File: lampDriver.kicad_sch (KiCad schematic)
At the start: 70 parts, among them IC8 1ED44175N01BXTSA1, Q2 BC847, Q4 BC807, T4 IMBG120R181M2HXTMA1, U1 OPA2356AIDGKR, U3 LM2901

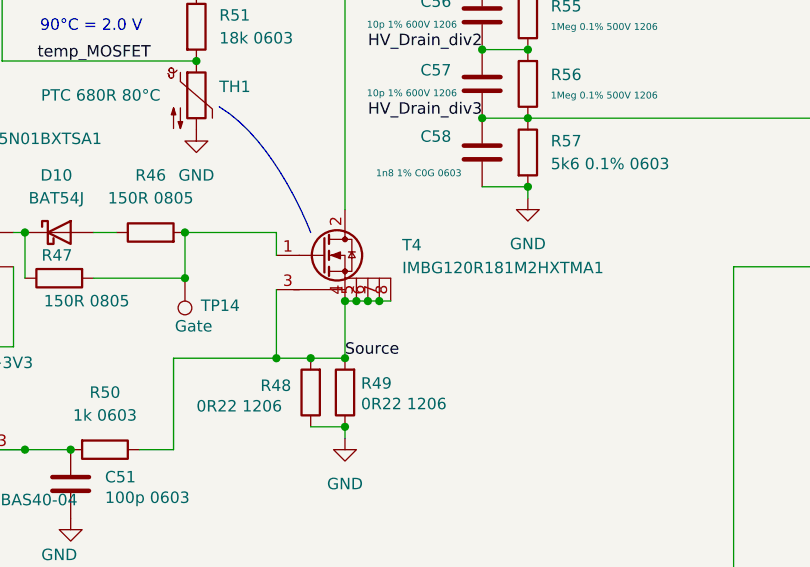
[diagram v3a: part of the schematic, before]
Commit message: changed to THT MOSFET
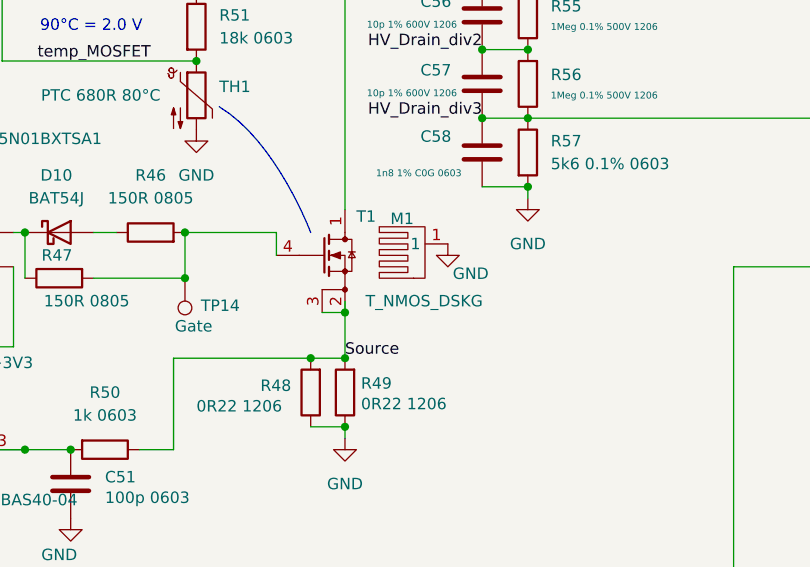
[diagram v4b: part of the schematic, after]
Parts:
- removed T4: IMBG120R181M2HXTMA1, Hansmann:TO-263-7_TabPin2_HV, symbol Hansmann:NMOS_GDS-KS_SMD
- added M1: ~, Hansmann_Kühlkörper:FK 274 MI 247 V, symbol Hansmann_Kühlkörper:Kühlkörper_mit_Pins
- added T1: T_NMOS_DSKG, Package_TO_SOT_THT:TO-247-4_Vertical, symbol Hansmann_Transistoren:Q_NMOS_DSKG
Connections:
- net GND: now also M1.1
- net HV_Drain: now also T1.1 (D)
- net Source: now also T1.2 (S), T1.3 (K)
- net at R46.2, R47.2, TP14.1: now also T1.4 (G)
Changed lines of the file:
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@@
 	)
 	(junction
-		(at 127 91.44)
-		(diameter 0)
-		(color 0 0 0 0)
-	)
-	(junction
-		(at 119.38 97.79)
-		(diameter 0)
-		(color 0 0 0 0)
-	)
-	(junction
 		(at 109.22 83.82)
 		(diameter 0)
@@
 	)
 	(junction
-		(at 130.81 91.44)
-		(diameter 0)
-		(color 0 0 0 0)
-	)
-	(junction
 		(at 123.19 137.16)
 		(diameter 0)
@@
 	)
 	(junction
-		(at 128.27 91.44)
-		(diameter 0)
-		(color 0 0 0 0)
-	)
-	(junction
-		(at 129.54 91.44)
-		(diameter 0)
-		(color 0 0 0 0)
-	)
-	(junction
 		(at 91.44 107.95)
 		(diameter 0)
@@
 	)
 	(junction
+		(at 127 92.71)
+		(diameter 0)
+		(color 0 0 0 0)
+	)
+	(junction
 		(at 242.57 86.36)
 		(diameter 0)
@@
 	(wire
 		(pts
-			(xy 130.81 91.44) (xy 132.08 91.44)
-		)
-		(stroke
-			(width 0)
-			(type default)
-		)
-	)
-	(wire
-		(pts
 			(xy 88.9 54.61) (xy 39.37 54.61)
 		)
@@
 	(wire
 		(pts
-			(xy 119.38 90.17) (xy 119.38 97.79)
-		)
-		(stroke
-			(width 0)
-			(type default)
-		)
-	)
-	(wire
-		(pts
 			(xy 99.06 158.75) (xy 100.33 158.75)
 		)
@@
 	(wire
 		(pts
-			(xy 107.95 97.79) (xy 119.38 97.79)
+			(xy 107.95 97.79) (xy 123.19 97.79)
 		)
 		(stroke
@@
 	(wire
 		(pts
-			(xy 127 91.44) (xy 128.27 91.44)
-		)
-		(stroke
-			(width 0)
-			(type default)
-		)
-	)
-	(wire
-		(pts
 			(xy 118.11 137.16) (xy 123.19 137.16)
 		)
@@
 	(wire
 		(pts
-			(xy 129.54 91.44) (xy 130.81 91.44)
-		)
-		(stroke
-			(width 0)
-			(type default)
-		)
-	)
-	(wire
-		(pts
 			(xy 194.31 46.99) (xy 190.5 46.99)
 		)
@@
 	(wire
 		(pts
-			(xy 127 91.44) (xy 127 97.79)
+			(xy 127 91.44) (xy 127 92.71)
 		)
 		(stroke
@@
 	(wire
 		(pts
-			(xy 119.38 97.79) (xy 123.19 97.79)
-		)
-		(stroke
-			(width 0)
-			(type default)
-		)
-	)
-	(wire
-		(pts
 			(xy 90.17 87.63) (xy 90.17 96.52)
 		)
@@
 	(wire
 		(pts
+			(xy 127 92.71) (xy 127 97.79)
+		)
+		(stroke
+			(width 0.254)
+			(type default)
+		)
+	)
+	(wire
+		(pts
 			(xy 246.38 66.04) (xy 252.73 66.04)
 		)
@@
 	(wire
 		(pts
+			(xy 124.46 92.71) (xy 127 92.71)
+		)
+		(stroke
+			(width 0.254)
+			(type default)
+		)
+	)
+	(wire
+		(pts
 			(xy 147.32 180.34) (xy 147.32 181.61)
 		)
@@
 	(wire
 		(pts
-			(xy 128.27 91.44) (xy 129.54 91.44)
-		)
-		(stroke
-			(width 0)
-			(type default)
-		)
-	)
-	(wire
-		(pts
 			(xy 214.63 100.33) (xy 215.9 100.33)
 		)
@@
 	)
 	(symbol
-		(lib_id "Hansmann:NMOS_GDS-KS_SMD")
-		(at 124.46 86.36 0)
-		(unit 1)
-		(exclude_from_sim no)
-		(in_bom yes)
-		(on_board yes)
-		(dnp no)
-		(fields_autoplaced yes)
-		(property "Reference" "T4"
-			(at 133.35 85.2169 0)
-			(effects
-				(font
-					(size 1.27 1.27)
-				)
-				(justify left)
-			)
-		)
-		(property "Value" "IMBG120R181M2HXTMA1"
-			(at 133.35 87.7569 0)
-			(effects
-				(font
-					(size 1.27 1.27)
-				)
-				(justify left)
-			)
-		)
-		(property "Footprint" "Hansmann:TO-263-7_TabPin2_HV"
-			(at 129.54 83.82 0)
-			(effects
-				(font
-					(size 1.27 1.27)
-				)
-				(hide yes)
-			)
-		)
-		(property "Datasheet" ""
-			(at 124.46 86.36 0)
-			(effects
-				(font
-					(size 1.27 1.27)
-				)
-				(hide yes)
-			)
-		)
-		(property "Description" "N-MOSFET transistor, gate/drain/source"
-			(at 124.46 86.36 0)
-			(effects
-				(font
-					(size 1.27 1.27)
-				)
-				(hide yes)
-			)
-		)
-		(pin "3"
-		)
-		(pin "6"
-		)
-		(pin "8"
-		)
-		(pin "7"
-		)
-		(pin "5"
-		)
-		(pin "4"
-		)
-		(pin "1"
-		)
-		(pin "2"
-		)
-		(instances
-			(project ""
-				(path "/c6e900e0-9399-44f0-8089-9dd7b8ffe54c/9b3070c3-43e0-4d43-9da1-9bc1bd2d6fb9/8926c1e3-dcc6-4ec7-96ae-5bdb4f87d364"
-					(reference "T4")
-					(unit 1)
-				)
-			)
-		)
-	)
-	(symbol
 		(lib_id "power:+3V3")
 		(at 218.44 39.37 0)
@@
 	)
 	(symbol
+		(lib_id "Hansmann_Kühlkörper:Kühlkörper_mit_Pins")
+		(at 134.62 85.09 180)
+		(unit 1)
+		(exclude_from_sim no)
+		(in_bom yes)
+		(on_board yes)
+		(dnp no)
+		(property "Reference" "M1"
+			(at 133.35 82.296 0)
+			(effects
+				(font
+					(size 1.27 1.27)
+				)
+			)
+		)
+		(property "Value" "~"
+			(at 133.35 81.28 0)
+			(effects
+				(font
+					(size 1.27 1.27)
+				)
+			)
+		)
+		(property "Footprint" "Hansmann_Kühlkörper:FK 274 MI 247 V"
+			(at 134.62 85.09 0)
+			(effects
+				(font
+					(size 1.27 1.27)
+				)
+				(hide yes)
+			)
+		)
+		(property "Datasheet" ""
+			(at 134.62 85.09 0)
+			(effects
+				(font
+					(size 1.27 1.27)
+				)
+				(hide yes)
+			)
+		)
+		(property "Description" ""
+			(at 134.62 85.09 0)
+			(effects
+				(font
+					(size 1.27 1.27)
+				)
+				(hide yes)
+			)
+		)
+		(pin "1"
+		)
+		(instances
+			(project ""
+				(path "/c6e900e0-9399-44f0-8089-9dd7b8ffe54c/9b3070c3-43e0-4d43-9da1-9bc1bd2d6fb9/8926c1e3-dcc6-4ec7-96ae-5bdb4f87d364"
+					(reference "M1")
+					(unit 1)
+				)
+			)
+		)
+	)
+	(symbol
 		(lib_id "Device:R")
 		(at 201.93 76.2 180)
@@
 	)
 	(symbol
+		(lib_id "Hansmann_Transistoren:Q_NMOS_DSKG")
+		(at 124.46 86.36 0)
+		(unit 1)
+		(exclude_from_sim no)
+		(in_bom yes)
+		(on_board yes)
+		(dnp no)
+		(property "Reference" "T1"
+			(at 128.27 82.042 0)
+			(effects
+				(font
+					(size 1.27 1.27)
+				)
+				(justify left)
+			)
+		)
+		(property "Value" "T_NMOS_DSKG"
+			(at 129.286 91.44 0)
+			(effects
+				(font
+					(size 1.27 1.27)
+				)
+				(justify left)
+			)
+		)
+		(property "Footprint" "Package_TO_SOT_THT:TO-247-4_Vertical"
+			(at 129.54 83.82 0)
+			(effects
+				(font
+					(size 1.27 1.27)
+				)
+				(hide yes)
+			)
+		)
+		(property "Datasheet" "~"
+			(at 124.46 86.36 0)
+			(effects
+				(font
+					(size 1.27 1.27)
+				)
+				(hide yes)
+			)
+		)
+		(property "Description" "N-MOSFET transistor, gate/drain/source"
+			(at 127.254 71.882 0)
+			(effects
+				(font
+					(size 1.27 1.27)
+				)
+				(hide yes)
+			)
+		)
+		(pin "3"
+		)
+		(pin "2"
+		)
+		(pin "4"
+		)
+		(pin "1"
+		)
+		(instances
+			(project ""
+				(path "/c6e900e0-9399-44f0-8089-9dd7b8ffe54c/9b3070c3-43e0-4d43-9da1-9bc1bd2d6fb9/8926c1e3-dcc6-4ec7-96ae-5bdb4f87d364"
+					(reference "T1")
+					(unit 1)
+				)
+			)
+		)
+	)
+	(symbol
 		(lib_id "Device:R")
 		(at 241.3 62.23 0)
@@
 					(unit 1)
 				)
+			)
+		)
+	)
+	(symbol
+		(lib_id "power:GND")
+		(at 138.43 85.09 0)
+		(unit 1)
+		(exclude_from_sim no)
+		(in_bom yes)
+		(on_board yes)
+		(dnp no)
+		(property "Reference" "#PWR079"
+			(at 138.43 91.44 0)
+			(effects
+				(font
+					(size 1.27 1.27)
+				)
+				(hide yes)
+			)
+		)
+		(property "Value" "GND"
+			(at 140.97 88.392 0)
+			(effects
+				(font
+					(size 1.27 1.27)
+				)
+			)
+		)
+		(property "Footprint" ""
+			(at 138.43 85.09 0)
+			(effects
+				(font
+					(size 1.27 1.27)
+				)
+				(hide yes)
+			)
+		)
+		(property "Datasheet" ""
+			(at 138.43 85.09 0)
+			(effects
+				(font
+					(size 1.27 1.27)
+				)
+				(hide yes)
+			)
+		)
+		(property "Description" "Power symbol creates a global label with name \"GND\" , ground"
+			(at 138.43 85.09 0)
+			(effects
+				(font
+					(size 1.27 1.27)
+				)
+				(hide yes)
+			)
+		)
+		(pin "1"
+		)
+		(instances
+			(project "OSLUV"
+				(path "/c6e900e0-9399-44f0-8089-9dd7b8ffe54c/9b3070c3-43e0-4d43-9da1-9bc1bd2d6fb9/8926c1e3-dcc6-4ec7-96ae-5bdb4f87d364"
+					(reference "#PWR079")
+					(unit 1)
+				)

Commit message: Rev. 1.0.0 production data
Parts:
- removed C17: 100p 0603, Capacitor_SMD:C_0603_1608Metric, symbol Device:C
- removed C5: 10µ X7R 50V 1210, Capacitor_SMD:C_1210_3225Metric, symbol Device:C
- removed D15: BAS40-04, Package_TO_SOT_SMD:SOT-23, symbol Diode:BAS40-04
- removed Q2: BC847, Package_TO_SOT_SMD:SOT-23, symbol Transistor_BJT:BC847
- removed Q4: BC807, Package_TO_SOT_SMD:SOT-23, symbol Transistor_BJT:Q_PNP_BEC
- removed R29, R69: 10k 0603, Resistor_SMD:R_0603_1608Metric, symbol Device:R
- removed R56: 1Meg 0.1% 500V 1206, Resistor_SMD:R_1206_3216Metric, symbol Device:R
- removed R67: 1k 0603, Resistor_SMD:R_0603_1608Metric, symbol Device:R
- removed R68: 3k3 0603, Resistor_SMD:R_0603_1608Metric, symbol Device:R
- added C42: 220µ 35V, Capacitor_THT:CP_Radial_D8.0mm_P3.50mm, symbol Device:C_Polarized
- added C44: 100n 0603, Capacitor_SMD:C_0603_1608Metric, symbol Device:C
- added C56: 10µ X7R 50V 1210, Capacitor_SMD:C_1210_3225Metric, symbol Device:C
- added D16, D18: BAT54J, Diode_SMD:D_SOD-323F, symbol Diode:BAT54J
- added Q4, Q5: DCX114EU-7-F, SOT65P210X110-6N, symbol Hansmann_Transistoren:DCX114EU-7-F
- added R57: 100k 0603, Resistor_SMD:R_0603_1608Metric, symbol Device:R
- added R59: 10k 0603, Resistor_SMD:R_0603_1608Metric, symbol Device:R
- added R62: 1k 0603, Resistor_SMD:R_0603_1608Metric, symbol Device:R
- added TP11: OCP, TestPoint:TestPoint_Pad_D1.0mm, symbol Connector:TestPoint
- added VR1: TC33X-2-103E, TC33X2503E, symbol Hansmann_Potis:TC33X-2-103E
- C51: renamed from C58; value 1n8 1% C0G 0603 -> 1n 1% C0G 0603
- C55: renamed from C4; value 100n 0603 -> 1u 0603
- C57: value 10p 1% 600V 1206 -> 100p 0603; footprint Capacitor_SMD:C_1206_3216Metric -> Capacitor_SMD:C_0603_1608Metric
- R69: renamed from R57; value 5k6 0.1% 0603 -> 12k 0.1% 0603
- R80: renamed from R66; value 3k9 0603 -> 18k 0603
- R81: renamed from R77; value 100k 0603 -> DNP
- R82: renamed from R74; value 1k 0603 -> 10k 0603
- renumbered C49 to C40, C3 to C41, C50 to C43, C52 to C45, C61 to C46, C53 to C47, C51 to C48, C55 to C49, C56 to C50, C40 to C52, C59 to C53, D10 to D17, D16 to D19, D17 to D20, D22 to D21, L6 to L5, L1 to L6, R75 to R52, R76 to R53, R44 to R54, R60 to R55, R62 to R56, R63 to R58, R47 to R60, R50 to R61, R46 to R63, R51 to R64, R49 to R65, R48 to R66, R54 to R67, R55 to R68, R79 to R70, R52 to R71, R53 to R72, R70 to R73, R71 to R74, R73 to R75, R58 to R76, R65 to R77, R59 to R78, R61 to R79, TP14 to TP10, TP2 to TP12, TP11 to TP13, TP12 to TP14, TP10 to TP8, TP13 to TP9, U3 to U1, U1 to U3
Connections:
- net +15V: now also C44.1
- net +3V3: now also D16.1 (K), Q5.4 (COM2), R57.1
- net GND: now also C57.2, C42.2, C44.2, C56.2, Q4.1 (COM1), Q5.1 (COM1), VR1.1
- net HV_Drain_div2: now also C51.1, R69.1, U3.5 (+); no longer C57.1
- net Isense_MOS: now also C57.1, D16.2 (A), R59.1
- net OCP: now also D18.1 (K), Q5.5 (IN2), Q5.6 (OUT1), TP11.1; no longer IC8.5 (EN/~{FLT}), U1.13
- net VDC_power: now also C42.1, C56.1
- removed net HV_Drain_div3: C51.1, C57.2, R69.1, U3.5 (+)
- new net: Q4.6 (OUT1), Q5.2 (IN1), R62.2
- new net: Q5.3 (OUT2), R62.1
- new net: R59.2, VR1.2, VR1.3
- new net: D18.2 (A), IC8.5 (EN/~{FLT}), R57.2, U1.13
- new net OCP_RESET: Q4.2 (IN1)
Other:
- moved on the sheet: TP14

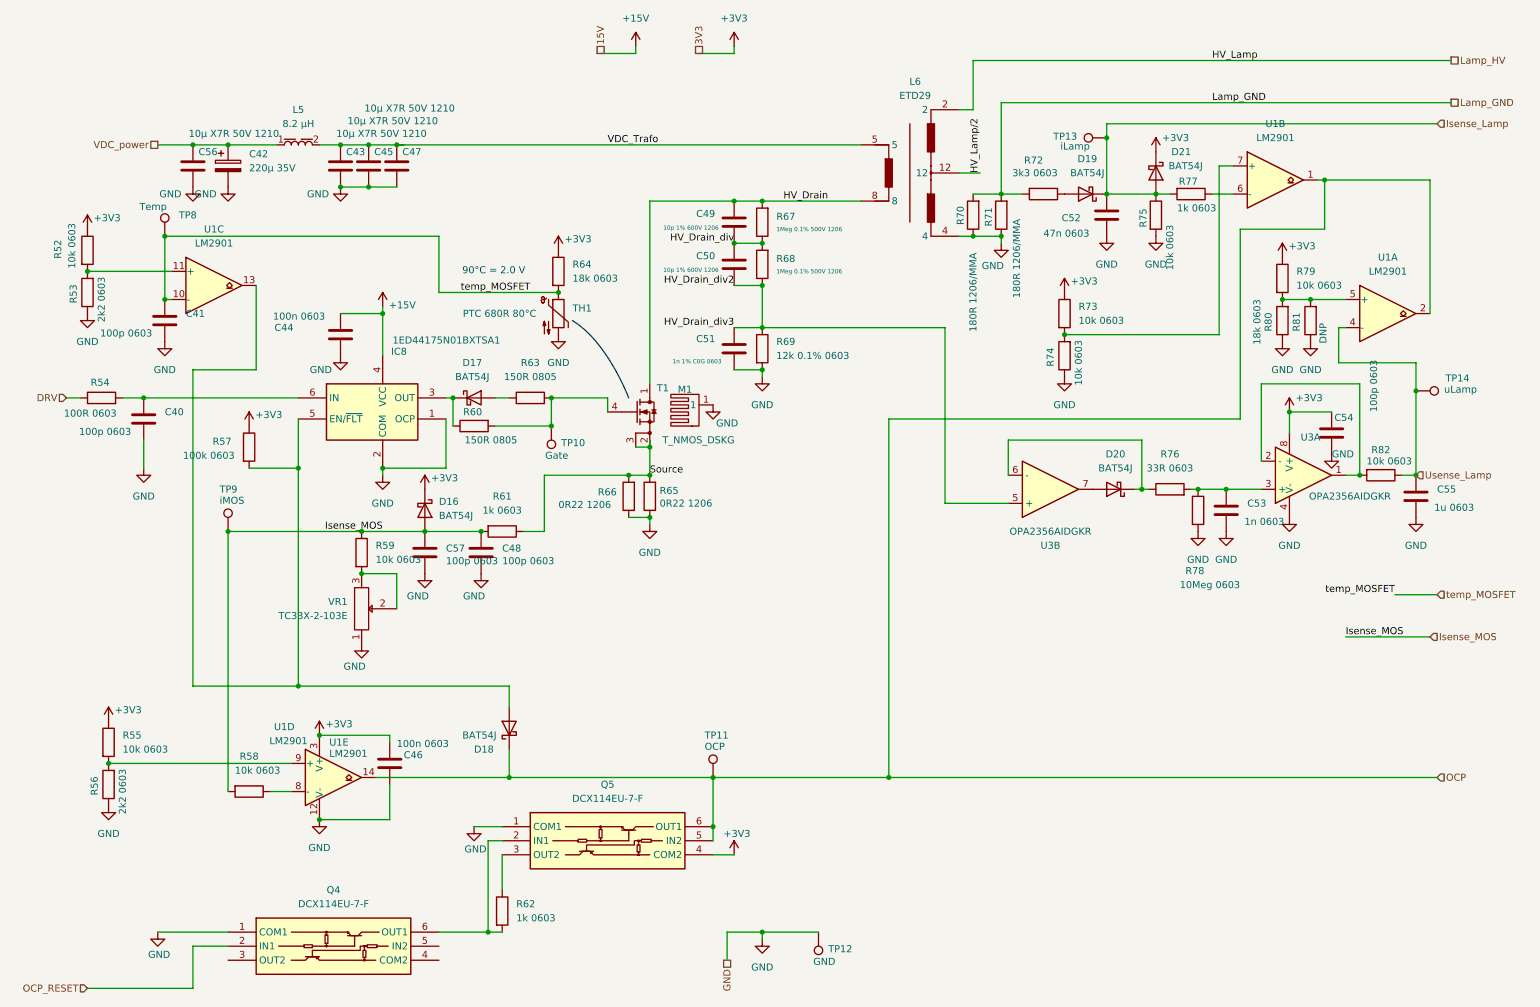
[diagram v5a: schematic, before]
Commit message: Rev 1.0.0 corrected component values
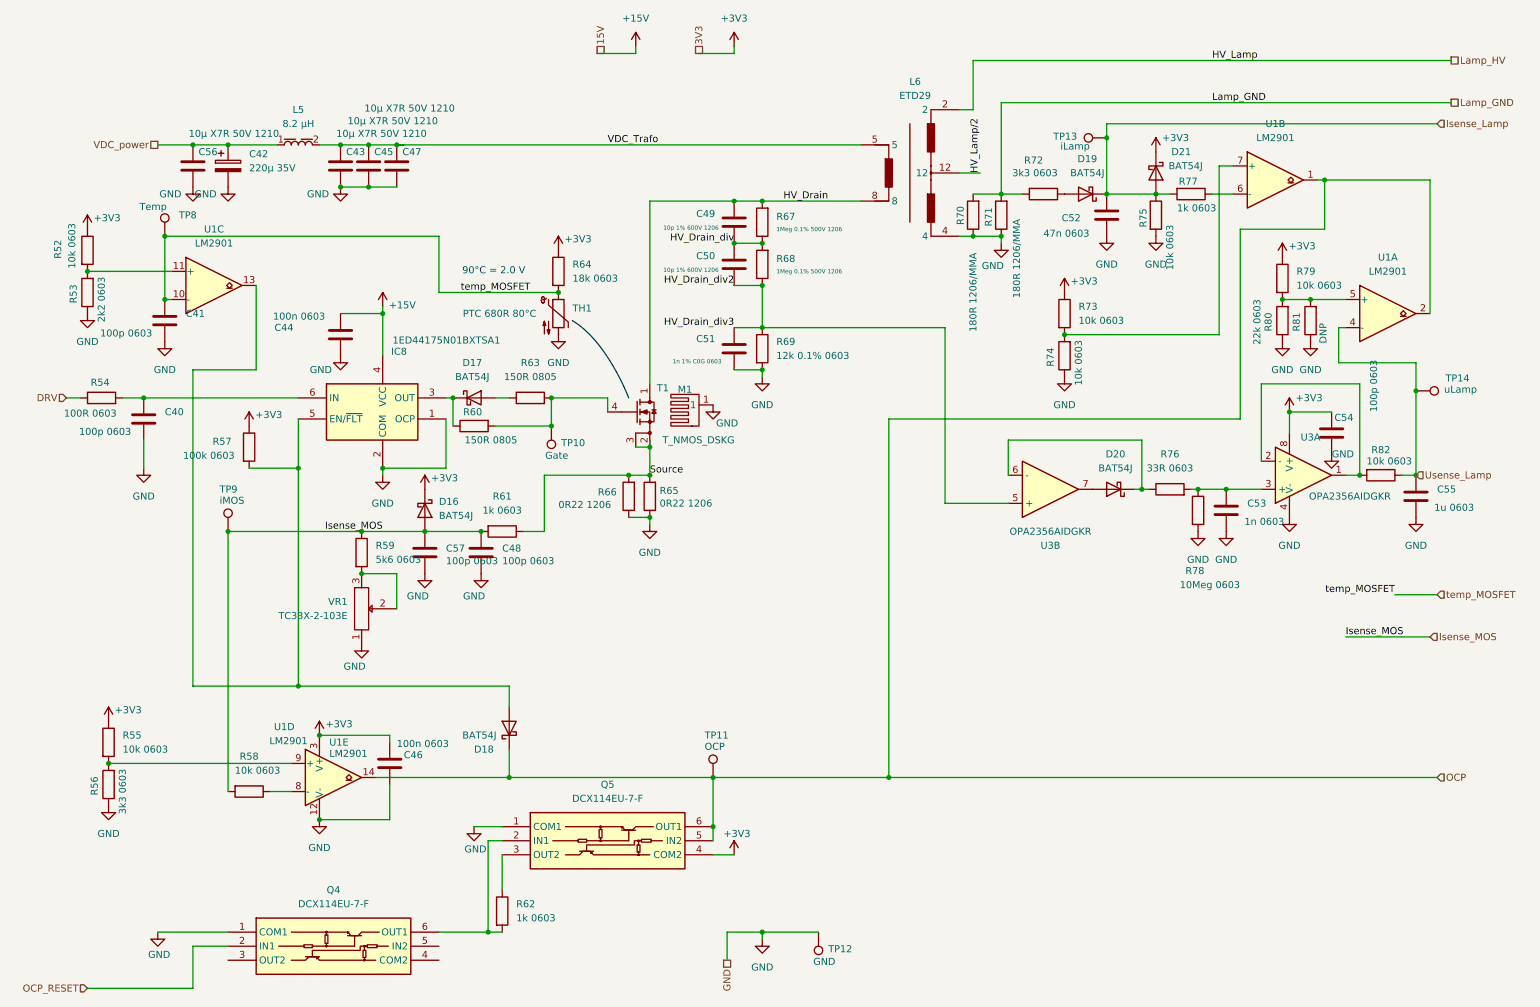
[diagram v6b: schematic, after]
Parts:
- R56: value 2k2 0603 -> 3k3 0603
- R59: value 10k 0603 -> 5k6 0603
- R80: value 18k 0603 -> 22k 0603
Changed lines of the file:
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@@
 			)
 		)
-		(property "Value" "10k 0603"
+		(property "Value" "5k6 0603"
 			(at 77.47 113.0299 0)
 			(effects
@@
 			)
 		)
-		(property "Value" "18k 0603"
+		(property "Value" "22k 0603"
 			(at 236.728 70.104 90)
 			(effects
@@
 			)
 		)
-		(property "Value" "2k2 0603"
+		(property "Value" "3k3 0603"
 			(at 31.75 154.94 90)
 			(effects
